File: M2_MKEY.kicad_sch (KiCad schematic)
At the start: 0 parts

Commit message: finished schematic draft and started placing components
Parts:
- added C1089, C50: 220nF/16V, A_HDJ_Library:C_0402_1005Metric, symbol Device:C_Small
- added C1090, C53: 10uF/10V, A_HDJ_Library:C_0402_1005Metric, symbol Device:C
- added C1091, C54: 100nF/16V, A_HDJ_Library:C_0402_1005Metric, symbol Device:C
- added D1018: LED_G, A_HDJ_Library:LED_0603_1608Metric, symbol Device:LED
- added H7: MountingHole_M2.0, A_HDJ_Library:MountingHole_2.75mm_M2_4.4mm_Pad_TopOnly, symbol Mechanical:MountingHole_Pad
- added J1007: Bus_M.2_Socket_M, A_HDJ_Library:PCIe_M.2_Connectors_P=0.5mm_H=4.2mm_KeyM, symbol Connector:Bus_M.2_Socket_M
- added R1060, R1062: 0R/1%, A_HDJ_Library:R_0402_1005Metric, symbol Device:R
- added R1061, R1063: 0R/1%, A_DFRobot:R_0402, symbol Device:R
- added R1064: 2.2K/1%, A_DFRobot:R_0402, symbol Device:R
- added TP2: TestPoint, A_HDJ_Library:TestPoint_Pad_D1.5mm, symbol Connector:TestPoint
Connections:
- new net: D1018.2 (A), R1064.1
- new net: D1018.1 (K), J1007.10 (DAS/~{DSS}/~{LED1})
- new net: J1007.69 (PEDET), R1062.1
- new net: J1007.52 (~{CLKREQ}), R1060.2, R1061.1
- new net: J1007.38 (DEVSLP), TP2.1
- new net: J1007.68 (SUSCLK), R1063.1
- new net +3V3: C1090.2, C1091.2, C53.2, C54.2, J1007.12 (3.3V), J1007.14 (3.3V), J1007.16 (3.3V), J1007.18 (3.3V), J1007.2 (3.3V), J1007.4 (3.3V), J1007.70 (3.3V), J1007.72 (3.3V), J1007.74 (3.3V), R1064.2
- new net CON_PCIE_TX_1+: C1089.2, J1007.49 (PETp0/SATA-A+)
- new net CON_PCIE_TX_1-: C50.2, J1007.47 (PETn0/SATA-A-)
- new net GND: C1090.1, C1091.1, C53.1, C54.1, H7.1, J1007.1 (GND), J1007.15 (GND), J1007.21 (GND), J1007.27 (GND), J1007.3 (GND), J1007.33 (GND), J1007.39 (GND), J1007.45 (GND), J1007.51 (GND), J1007.57 (GND), J1007.71 (GND), J1007.73 (GND), J1007.75 (GND), J1007.9 (GND), J1007.MP1, J1007.MP2, R1061.2, R1062.2
- new net PCIE_RX_1+: J1007.43 (PERp0/SATA-B-)
- new net PCIE_RX_1-: J1007.41 (PERn0/SATA-B+)
- new net PCIE_TX_1+: C1089.1
- new net PCIE_TX_1-: C50.1
- new net REFCLKM+: J1007.55 (REFCLKp)
- new net REFCLKM-: J1007.53 (REFCLKn)
- new net SUSCLK: R1063.2
- new net ~{CLKREQM}: R1060.1
- new net ~{PLT_RST}: J1007.50 (~{PERST})
- new net ~{WAKE}: J1007.54 (~{PEWAKE})
- no-connect marks 0 -> 12
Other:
- note added: "32.768kHz clock for low power"
- note added: "SSD active LED"
- note added: "To be grounded for SATA, No Connect for PCIe"

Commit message: commit before removing duplicated glasgow
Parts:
- H5: renamed from H7; footprint A_HDJ_Library:MountingHole_2.75mm_M2_4.4mm_Pad_TopOnly -> MountingHole:MountingHole_2.7mm_Pad_TopOnly
- renumbered C1089 to C88, C50 to C89, C1090 to C90, C1091 to C91, C53 to C92, C54 to C93, D1018 to D7, J1007 to J24, R1060 to R36, R1061 to R37, R1062 to R38, R1063 to R39, R1064 to R40, TP2 to TP3
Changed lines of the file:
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@@
 		(on_board yes)
 		(dnp no)
-		(property "Reference" "C1091"
+		(property "Reference" "C91"
 			(at 139.7 34.29 90)
 			(effects
@@
 			(project "microcyber"
 				(path "/7ac319af-771c-4997-a005-b73a4a9b44ab/0f85bef4-33ba-41bd-b468-8a14848b6d64"
-					(reference "C1091")
+					(reference "C91")
 					(unit 1)
 				)
@@
 		(dnp no)
 		(fields_autoplaced yes)
-		(property "Reference" "#PWR01075"
+		(property "Reference" "#PWR096"
 			(at 128.27 30.48 0)
 			(effects
@@
 			(project "microcyber"
 				(path "/7ac319af-771c-4997-a005-b73a4a9b44ab/0f85bef4-33ba-41bd-b468-8a14848b6d64"
-					(reference "#PWR01075")
+					(reference "#PWR096")
 					(unit 1)
 				)
@@
 		(on_board yes)
 		(dnp no)
-		(property "Reference" "R1064"
+		(property "Reference" "R40"
 			(at 171.45 97.79 0)
 			(effects
@@
 			(project "microcyber"
 				(path "/7ac319af-771c-4997-a005-b73a4a9b44ab/0f85bef4-33ba-41bd-b468-8a14848b6d64"
-					(reference "R1064")
+					(reference "R40")
 					(unit 1)
 				)
@@
 		(on_board yes)
 		(dnp no)
-		(property "Reference" "C1089"
+		(property "Reference" "C88"
 			(at 67.31 66.04 90)
 			(effects
@@
 			(project "microcyber"
 				(path "/7ac319af-771c-4997-a005-b73a4a9b44ab/0f85bef4-33ba-41bd-b468-8a14848b6d64"
-					(reference "C1089")
+					(reference "C88")
 					(unit 1)
 				)
@@
 		(dnp no)
 		(fields_autoplaced yes)
-		(property "Reference" "D1018"
+		(property "Reference" "D7"
 			(at 170.18 106.9975 90)
 			(effects
@@
 			(project "microcyber"
 				(path "/7ac319af-771c-4997-a005-b73a4a9b44ab/0f85bef4-33ba-41bd-b468-8a14848b6d64"
-					(reference "D1018")
+					(reference "D7")
 					(unit 1)
 				)
@@
 		(on_board no)
 		(dnp yes)
-		(property "Reference" "R1062"
+		(property "Reference" "R38"
 			(at 170.18 121.92 90)
 			(effects
@@
 			(project "microcyber"
 				(path "/7ac319af-771c-4997-a005-b73a4a9b44ab/0f85bef4-33ba-41bd-b468-8a14848b6d64"
-					(reference "R1062")
+					(reference "R38")
 					(unit 1)
 				)
@@
 		(on_board yes)
 		(dnp no)
-		(property "Reference" "C50"
+		(property "Reference" "C89"
 			(at 67.31 68.58 90)
 			(effects
@@
 			(project "microcyber"
 				(path "/7ac319af-771c-4997-a005-b73a4a9b44ab/0f85bef4-33ba-41bd-b468-8a14848b6d64"
-					(reference "C50")
+					(reference "C89")
 					(unit 1)
 				)
@@
 		(on_board yes)
 		(dnp yes)
-		(property "Reference" "R1060"
+		(property "Reference" "R36"
 			(at 83.82 60.96 90)
 			(effects
@@
 			(project "microcyber"
 				(path "/7ac319af-771c-4997-a005-b73a4a9b44ab/0f85bef4-33ba-41bd-b468-8a14848b6d64"
-					(reference "R1060")
+					(reference "R36")
 					(unit 1)
 				)
@@
 		(on_board yes)
 		(dnp no)
-		(property "Reference" "C53"
+		(property "Reference" "C92"
 			(at 139.7 40.64 90)
 			(effects
@@
 			(project "microcyber"
 				(path "/7ac319af-771c-4997-a005-b73a4a9b44ab/0f85bef4-33ba-41bd-b468-8a14848b6d64"
-					(reference "C53")
+					(reference "C92")
 					(unit 1)
 				)
@@
 		(dnp no)
 		(fields_autoplaced yes)
-		(property "Reference" "#PWR01080"
+		(property "Reference" "#PWR0101"
 			(at 193.04 85.09 0)
 			(effects
@@
 			(project "microcyber"
 				(path "/7ac319af-771c-4997-a005-b73a4a9b44ab/0f85bef4-33ba-41bd-b468-8a14848b6d64"
-					(reference "#PWR01080")
+					(reference "#PWR0101")
 					(unit 1)
 				)
@@
 		(dnp no)
 		(fields_autoplaced yes)
-		(property "Reference" "J1007"
+		(property "Reference" "J24"
 			(at 130.4641 49.53 0)
 			(effects
@@
 			(project "microcyber"
 				(path "/7ac319af-771c-4997-a005-b73a4a9b44ab/0f85bef4-33ba-41bd-b468-8a14848b6d64"
-					(reference "J1007")
+					(reference "J24")
 					(unit 1)
 				)
@@
 		(dnp no)
 		(fields_autoplaced yes)
-		(property "Reference" "#PWR01078"
+		(property "Reference" "#PWR099"
 			(at 166.37 99.06 0)
 			(effects
@@
 			(project "microcyber"
 				(path "/7ac319af-771c-4997-a005-b73a4a9b44ab/0f85bef4-33ba-41bd-b468-8a14848b6d64"
-					(reference "#PWR01078")
+					(reference "#PWR099")
 					(unit 1)
 				)
@@
 		(dnp no)
 		(fields_autoplaced yes)
-		(property "Reference" "#PWR01077"
+		(property "Reference" "#PWR098"
 			(at 152.4 39.37 0)
 			(effects
@@
 			(project "microcyber"
 				(path "/7ac319af-771c-4997-a005-b73a4a9b44ab/0f85bef4-33ba-41bd-b468-8a14848b6d64"
-					(reference "#PWR01077")
+					(reference "#PWR098")
 					(unit 1)
 				)
@@
 		(dnp no)
 		(fields_autoplaced yes)
-		(property "Reference" "#PWR01079"
+		(property "Reference" "#PWR0100"
 			(at 181.61 120.65 0)
 			(effects
@@
 			(project "microcyber"
 				(path "/7ac319af-771c-4997-a005-b73a4a9b44ab/0f85bef4-33ba-41bd-b468-8a14848b6d64"
-					(reference "#PWR01079")
+					(reference "#PWR0100")
 					(unit 1)
 				)
@@
 		(on_board yes)
 		(dnp no)
-		(property "Reference" "TP2"
+		(property "Reference" "TP3"
 			(at 96.774 123.19 90)
 			(effects
@@
 			(project "microcyber"
 				(path "/7ac319af-771c-4997-a005-b73a4a9b44ab/0f85bef4-33ba-41bd-b468-8a14848b6d64"
-					(reference "TP2")
+					(reference "TP3")
 					(unit 1)
 				)
@@
 		(dnp no)
 		(fields_autoplaced yes)
-		(property "Reference" "#PWR01076"
+		(property "Reference" "#PWR097"
 			(at 128.27 154.94 0)
 			(effects
@@
 			(project "microcyber"
 				(path "/7ac319af-771c-4997-a005-b73a4a9b44ab/0f85bef4-33ba-41bd-b468-8a14848b6d64"
-					(reference "#PWR01076")
+					(reference "#PWR097")
 					(unit 1)
 				)
@@
 		(dnp no)
 		(fields_autoplaced yes)
-		(property "Reference" "H7"
+		(property "Reference" "H5"
 			(at 195.58 73.66 0)
 			(effects
@@
 			)
 		)
-		(property "Footprint" "A_HDJ_Library:MountingHole_2.75mm_M2_4.4mm_Pad_TopOnly"
+		(property "Footprint" "MountingHole:MountingHole_2.7mm_Pad_TopOnly"
 			(at 193.04 76.2 0)
 			(effects
@@
 			(project "microcyber"
 				(path "/7ac319af-771c-4997-a005-b73a4a9b44ab/0f85bef4-33ba-41bd-b468-8a14848b6d64"
-					(reference "H7")
+					(reference "H5")
 					(unit 1)
 				)
@@
 		(dnp no)
 		(fields_autoplaced yes)
-		(property "Reference" "#PWR01074"
+		(property "Reference" "#PWR095"
 			(at 90.17 38.1 0)
 			(effects
@@
 			(project "microcyber"
 				(path "/7ac319af-771c-4997-a005-b73a4a9b44ab/0f85bef4-33ba-41bd-b468-8a14848b6d64"
-					(reference "#PWR01074")
+					(reference "#PWR095")
 					(unit 1)
 				)
@@
 		(on_board yes)
 		(dnp no)
-		(property "Reference" "C54"
+		(property "Reference" "C93"
 			(at 139.7 46.99 90)
 			(effects
@@
 			(project "microcyber"
 				(path "/7ac319af-771c-4997-a005-b73a4a9b44ab/0f85bef4-33ba-41bd-b468-8a14848b6d64"
-					(reference "C54")
+					(reference "C93")
 					(unit 1)
 				)
@@
 		(on_board yes)
 		(dnp no)
-		(property "Reference" "C1090"
+		(property "Reference" "C90"
 			(at 139.7 27.94 90)
 			(effects
@@
 			(project "microcyber"
 				(path "/7ac319af-771c-4997-a005-b73a4a9b44ab/0f85bef4-33ba-41bd-b468-8a14848b6d64"
-					(reference "C1090")
+					(reference "C90")
 					(unit 1)
 				)
@@
 		(on_board yes)
 		(dnp no)
-		(property "Reference" "R1061"
+		(property "Reference" "R37"
 			(at 96.52 44.45 0)
 			(effects
@@
 			(project "microcyber"
 				(path "/7ac319af-771c-4997-a005-b73a4a9b44ab/0f85bef4-33ba-41bd-b468-8a14848b6d64"
-					(reference "R1061")
+					(reference "R37")
 					(unit 1)
 				)
@@
 		(on_board yes)
 		(dnp no)
-		(property "Reference" "R1063"
+		(property "Reference" "R39"
 			(at 170.18 129.54 90)
 			(effects
@@
 			(project "microcyber"
 				(path "/7ac319af-771c-4997-a005-b73a4a9b44ab/0f85bef4-33ba-41bd-b468-8a14848b6d64"
-					(reference "R1063")
-					(unit 1)
-				)
+					(reference "R39")
+					(unit 1)
+				)

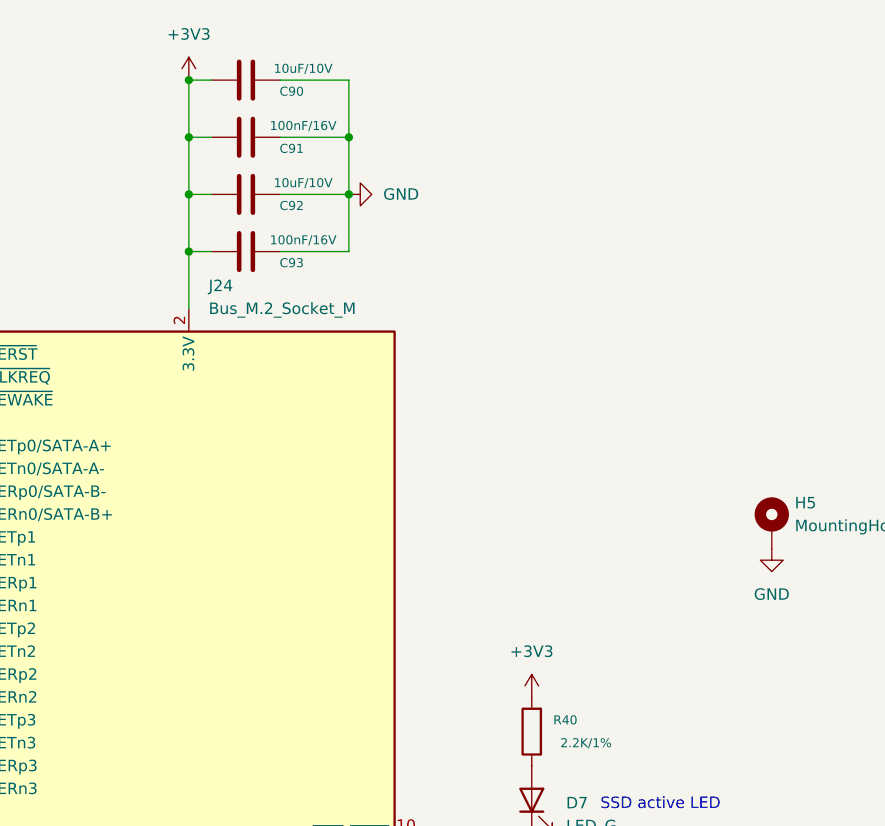
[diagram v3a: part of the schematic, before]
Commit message: fixed 5v->3v bug
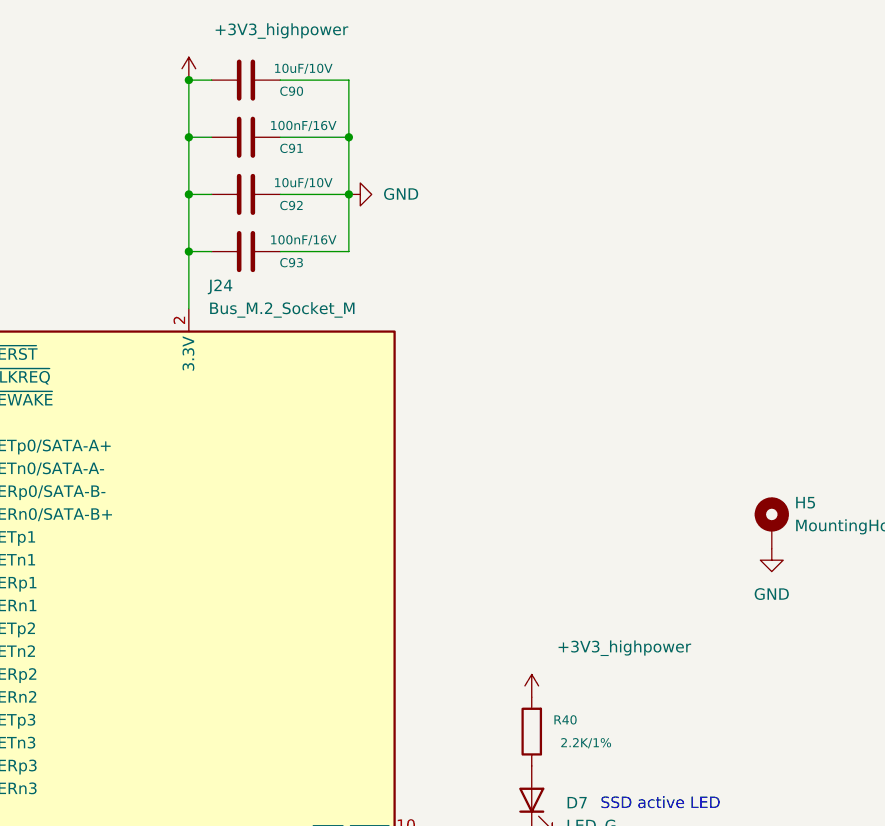
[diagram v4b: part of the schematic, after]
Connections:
- net +3V3 renamed +3V3_highpower
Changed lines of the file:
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@@
 		(in_pos_files yes)
 		(dnp no)
-		(fields_autoplaced yes)
 		(property "Reference" "#PWR096"
 			(at 128.27 30.48 0)
@@
 			)
 		)
-		(property "Value" "+3V3"
-			(at 128.27 21.59 0)
-			(show_name no)
-			(do_not_autoplace no)
-			(effects
-				(font
-					(size 1.27 1.27)
-				)
+		(property "Value" "+3V3_highpower"
+			(at 131.064 21.082 0)
+			(show_name no)
+			(do_not_autoplace no)
+			(effects
+				(font
+					(size 1.27 1.27)
+				)
+				(justify left)
 			)
 		)
@@
 	)
 	(symbol
-		(lib_id "power:+3V3")
-		(at 166.37 95.25 0)
-		(unit 1)
-		(body_style 1)
-		(exclude_from_sim no)
-		(in_bom yes)
-		(on_board yes)
-		(in_pos_files yes)
-		(dnp no)
-		(fields_autoplaced yes)
-		(property "Reference" "#PWR099"
-			(at 166.37 99.06 0)
-			(hide yes)
-			(show_name no)
-			(do_not_autoplace no)
-			(effects
-				(font
-					(size 1.27 1.27)
-				)
-			)
-		)
-		(property "Value" "+3V3"
-			(at 166.37 90.17 0)
-			(show_name no)
-			(do_not_autoplace no)
-			(effects
-				(font
-					(size 1.27 1.27)
-				)
-			)
-		)
-		(property "Footprint" ""
-			(at 166.37 95.25 0)
-			(hide yes)
-			(show_name no)
-			(do_not_autoplace no)
-			(effects
-				(font
-					(size 1.27 1.27)
-				)
-			)
-		)
-		(property "Datasheet" ""
-			(at 166.37 95.25 0)
-			(hide yes)
-			(show_name no)
-			(do_not_autoplace no)
-			(effects
-				(font
-					(size 1.27 1.27)
-				)
-			)
-		)
-		(property "Description" ""
-			(at 166.37 95.25 0)
-			(hide yes)
-			(show_name no)
-			(do_not_autoplace no)
-			(effects
-				(font
-					(size 1.27 1.27)
-				)
-			)
-		)
-		(pin "1"
-		)
-		(instances
-			(project "microcyber"
-				(path "/7ac319af-771c-4997-a005-b73a4a9b44ab/0f85bef4-33ba-41bd-b468-8a14848b6d64"
-					(reference "#PWR099")
-					(unit 1)
-				)
-			)
-		)
-	)
-	(symbol
 		(lib_id "power:GND")
 		(at 146.05 39.37 90)
@@
 					(unit 1)
 				)
+			)
+		)
+	)
+	(symbol
+		(lib_id "power:+3V3")
+		(at 166.37 95.25 0)
+		(unit 1)
+		(body_style 1)
+		(exclude_from_sim no)
+		(in_bom yes)
+		(on_board yes)
+		(in_pos_files yes)
+		(dnp no)
+		(property "Reference" "#PWR099"
+			(at 166.37 99.06 0)
+			(hide yes)
+			(show_name no)
+			(do_not_autoplace no)
+			(effects
+				(font
+					(size 1.27 1.27)
+				)
+			)
+		)
+		(property "Value" "+3V3_highpower"
+			(at 169.164 89.662 0)
+			(show_name no)
+			(do_not_autoplace no)
+			(effects
+				(font
+					(size 1.27 1.27)
+				)
+				(justify left)
+			)
+		)
+		(property "Footprint" ""
+			(at 166.37 95.25 0)
+			(hide yes)
+			(show_name no)
+			(do_not_autoplace no)
+			(effects
+				(font
+					(size 1.27 1.27)
+				)
+			)
+		)
+		(property "Datasheet" ""
+			(at 166.37 95.25 0)
+			(hide yes)
+			(show_name no)
+			(do_not_autoplace no)
+			(effects
+				(font
+					(size 1.27 1.27)
+				)
+			)
+		)
+		(property "Description" ""
+			(at 166.37 95.25 0)
+			(hide yes)
+			(show_name no)
+			(do_not_autoplace no)
+			(effects
+				(font
+					(size 1.27 1.27)
+				)
+			)
+		)
+		(pin "1"
+		)
+		(instances
+			(project "microcyber"
+				(path "/7ac319af-771c-4997-a005-b73a4a9b44ab/0f85bef4-33ba-41bd-b468-8a14848b6d64"
+					(reference "#PWR099")
+					(unit 1)
+				)

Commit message: last push before editing with the grid view (gonna break everything)
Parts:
- C88: value 220nF/16V -> 220n; DF_Comment 贴片电容0402-220nF-16V-X7R -> (none); MPN (none) -> GCM155R71C224KE02D
- C89: value 220nF/16V -> 220n; MPN (none) -> GCM155R71C224KE02D
- C90, C92: value 10uF/10V -> 10u; DF_Comment 贴片电容0402-10UF-10V-X5R_GRM155R61A106ME44D -> (none); MPN (none) -> MLASL168BB5106MTNB33
- C91, C93: value 100nF/16V -> u1; DF_Comment 贴片电容0402-100nF-16V-X7R(0402) -> (none); MPN (none) -> C0402C104J4RECAUTO
- D7: DF_Comment 贴片LED蓝色0603(0603) -> (none); MPN (none) -> 150060BS75000
- H5: now left out of the parts list
- J24: MPN (none) -> APCI0107-P001A
- R37: value 0R/1% -> 0; DF_Comment 贴片电阻0402-0R-1% -> (none); MPN (none) -> MCS0402HZ0000ZE100
- R39: value 0R/1% -> 0; DF_Comment 贴片电阻0402-0R-1% -> (none); MPN (none) -> C2889341
- R40: value 2.2K/1% -> 2K2; DF_Comment 贴片电阻0402-2.2K-1% -> (none); MPN (none) -> 560112110087
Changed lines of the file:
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@@
 			)
 		)
-		(property "Value" "100nF/16V"
+		(property "Value" "u1"
 			(at 140.97 31.75 90)
 			(show_name no)
@@
 			)
 		)
-		(property "Description" ""
+		(property "Description" "16v"
 			(at 134.62 33.02 0)
 			(hide yes)
@@
 			)
 		)
-		(property "DF_Comment" "贴片电容0402-100nF-16V-X7R(0402)"
+		(property "DF_Comment" ""
 			(at 134.62 33.02 0)
 			(hide yes)
@@
 			)
 		)
-		(property "Field-1" ""
+		(property "MPN" "C0402C104J4RECAUTO"
 			(at 134.62 33.02 0)
 			(hide yes)
@@
 			)
 		)
-		(property "Value" "2.2K/1%"
+		(property "Value" "2K2"
 			(at 175.26 100.33 0)
 			(show_name no)
@@
 			)
 		)
-		(property "Description" ""
+		(property "Description" "1%"
 			(at 166.37 99.06 0)
 			(hide yes)
@@
 			)
 		)
-		(property "DF_Comment" "贴片电阻0402-2.2K-1%"
+		(property "DF_Comment" ""
 			(at 166.37 99.06 0)
 			(hide yes)
@@
 			)
 		)
-		(property "Field-1" ""
+		(property "MPN" "560112110087"
 			(at 166.37 99.06 0)
 			(hide yes)
@@
 			)
 		)
-		(property "Value" "220nF/16V"
+		(property "Value" "220n"
 			(at 69.85 66.04 90)
 			(show_name no)
@@
 			)
 		)
-		(property "Description" ""
+		(property "Description" "16v"
 			(at 68.58 67.31 0)
 			(hide yes)
@@
 			)
 		)
-		(property "DF_Comment" "贴片电容0402-220nF-16V-X7R"
+		(property "DF_Comment" ""
 			(at 68.58 67.31 0)
 			(hide yes)
@@
 			)
 		)
-		(property "Field-1" ""
+		(property "MPN" "GCM155R71C224KE02D"
 			(at 68.58 67.31 0)
 			(hide yes)
@@
 			)
 		)
-		(property "Description" ""
+		(property "Description" "blue"
 			(at 166.37 106.68 0)
 			(hide yes)
@@
 			)
 		)
-		(property "DF_Comment" "贴片LED蓝色0603(0603)"
+		(property "DF_Comment" ""
 			(at 166.37 106.68 0)
 			(hide yes)
@@
 			)
 		)
-		(property "Field-1" ""
+		(property "MPN" "150060BS75000"
 			(at 166.37 106.68 0)
 			(hide yes)
@@
 			)
 		)
-		(property "Value" "220nF/16V"
+		(property "Value" "220n"
 			(at 69.85 68.58 90)
 			(show_name no)
@@
 			)
 		)
-		(property "Description" ""
+		(property "Description" "16v"
 			(at 68.58 69.85 0)
 			(hide yes)
@@
 			)
 		)
-		(property "Field-1" ""
+		(property "MPN" "GCM155R71C224KE02D"
 			(at 68.58 69.85 0)
 			(hide yes)
@@
 			)
 		)
-		(property "Value" "10uF/10V"
+		(property "Value" "10u"
 			(at 140.97 38.1 90)
 			(show_name no)
@@
 			)
 		)
-		(property "Description" ""
+		(property "Description" "10v"
 			(at 134.62 39.37 0)
 			(hide yes)
@@
 			)
 		)
-		(property "DF_Comment" "贴片电容0402-10UF-10V-X5R_GRM155R61A106ME44D"
+		(property "DF_Comment" ""
 			(at 134.62 39.37 0)
 			(hide yes)
@@
 			)
 		)
-		(property "Field-1" ""
+		(property "MPN" "MLASL168BB5106MTNB33"
 			(at 134.62 39.37 0)
 			(hide yes)
@@
 			)
 		)
-		(property "Field-1" ""
+		(property "MPN" "APCI0107-P001A"
 			(at 128.27 100.33 0)
 			(hide yes)
@@
 		(body_style 1)
 		(exclude_from_sim no)
-		(in_bom yes)
+		(in_bom no)
 		(on_board yes)
 		(in_pos_files yes)
@@
 			)
 		)
-		(property "Value" "100nF/16V"
+		(property "Value" "u1"
 			(at 140.97 44.45 90)
 			(show_name no)
@@
 			)
 		)
-		(property "Description" ""
+		(property "Description" "16v"
 			(at 134.62 45.72 0)
 			(hide yes)
@@
 			)
 		)
-		(property "DF_Comment" "贴片电容0402-100nF-16V-X7R(0402)"
+		(property "DF_Comment" ""
 			(at 134.62 45.72 0)
 			(hide yes)
@@
 			)
 		)
-		(property "Field-1" ""
+		(property "MPN" "C0402C104J4RECAUTO"
 			(at 134.62 45.72 0)
 			(hide yes)
@@
 			)
 		)
-		(property "Value" "10uF/10V"
+		(property "Value" "10u"
 			(at 140.97 25.4 90)
 			(show_name no)
@@
 			)
 		)
-		(property "Description" ""
+		(property "Description" "10v"
 			(at 134.62 26.67 0)
 			(hide yes)
@@
 			)
 		)
-		(property "DF_Comment" "贴片电容0402-10UF-10V-X5R_GRM155R61A106ME44D"
+		(property "DF_Comment" ""
 			(at 134.62 26.67 0)
 			(hide yes)
@@
 			)
 		)
-		(property "Field-1" ""
+		(property "MPN" "MLASL168BB5106MTNB33"
 			(at 134.62 26.67 0)
 			(hide yes)
@@
 			)
 		)
-		(property "Value" "0R/1%"
+		(property "Value" "0"
 			(at 97.79 46.99 0)
 			(show_name no)
@@
 			)
 		)
-		(property "Description" ""
+		(property "Description" "1%"
 			(at 90.17 48.26 0)
 			(hide yes)
@@
 			)
 		)
-		(property "DF_Comment" "贴片电阻0402-0R-1%"
+		(property "DF_Comment" ""
 			(at 90.17 48.26 0)
 			(hide yes)
@@
 			)
 		)
-		(property "Field-1" ""
+		(property "MPN" "MCS0402HZ0000ZE100"
 			(at 90.17 48.26 0)
 			(hide yes)
@@
 			)
 		)
-		(property "Value" "0R/1%"
+		(property "Value" "0"
 			(at 160.02 129.54 90)
 			(show_name no)
@@
 			)
 		)
-		(property "Description" ""
+		(property "Description" "1%"
 			(at 163.83 128.27 0)
 			(hide yes)
@@
 			)
 		)
-		(property "DF_Comment" "贴片电阻0402-0R-1%"
+		(property "DF_Comment" ""
 			(at 163.83 128.27 0)
 			(hide yes)
@@
 			)
 		)
-		(property "Field-1" ""
+		(property "MPN" "C2889341"
 			(at 163.83 128.27 0)
 			(hide yes)
